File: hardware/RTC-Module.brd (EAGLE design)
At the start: 19.1 x 19.1 mm, 15 parts, among them Q1 32.768kHz, U1 DS1307

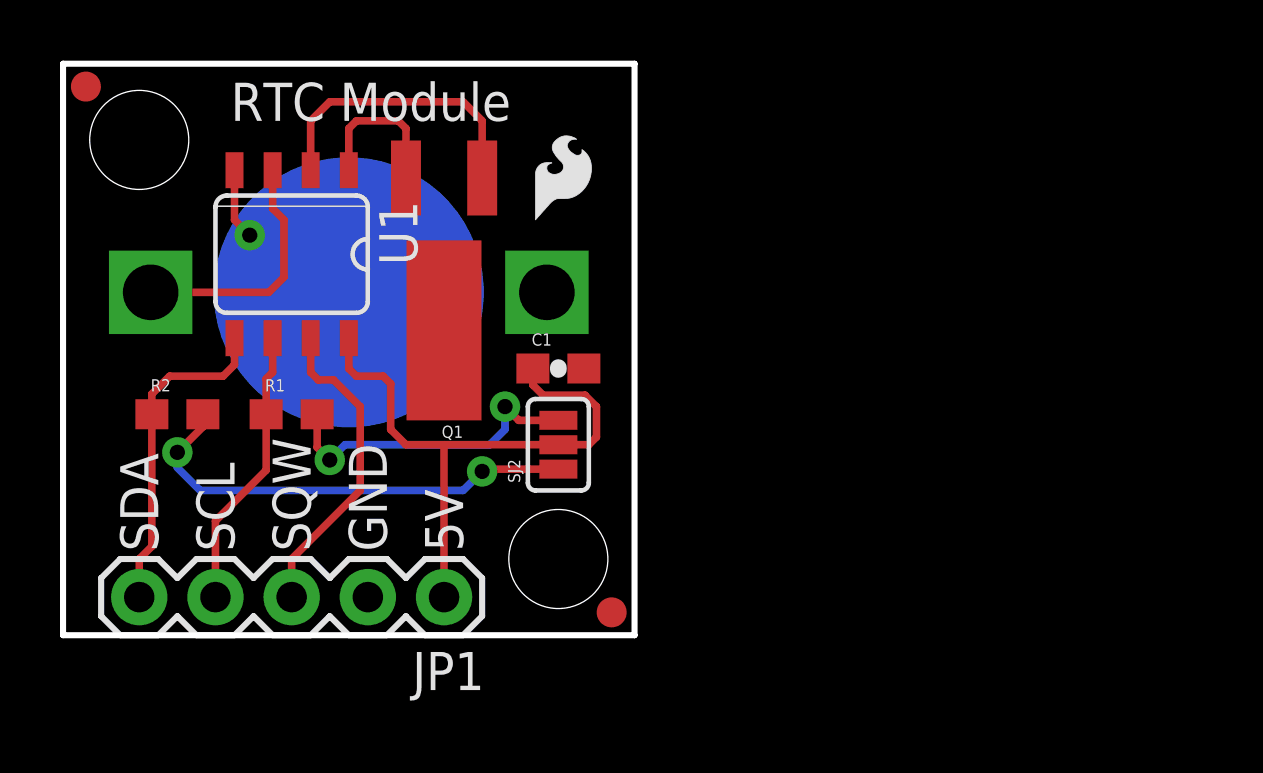
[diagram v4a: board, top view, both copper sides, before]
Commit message: Minor fixes
1.) added i2c address to sch
2.) added rev number in bottom copper
3.) updated revision info in sch and brd
4.) moved fiducials to clear drc
5.) cleaned up sda trace a bit
6.) added flame to bottom silk
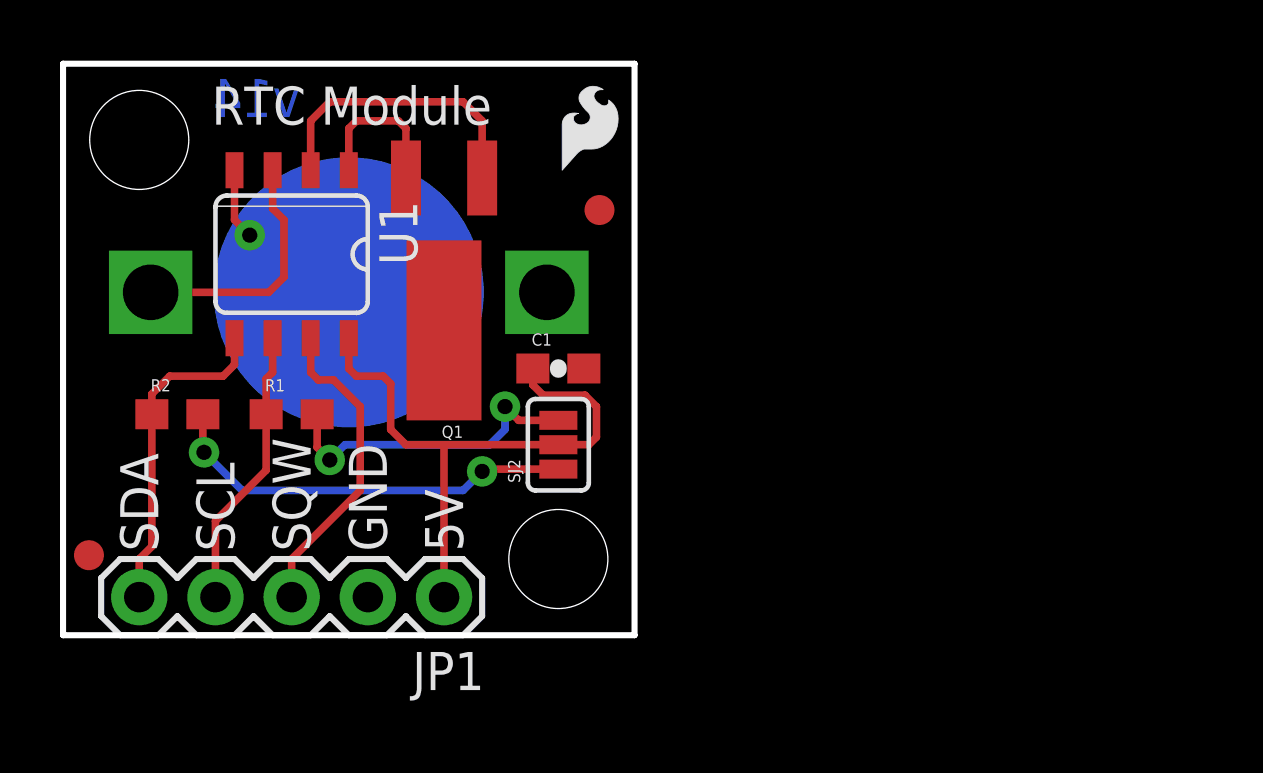
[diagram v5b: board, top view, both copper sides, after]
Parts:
- added U$2: LOGO-SFESK, SparkFun:SFE-LOGO-FLAME
- moved E$1 15.6 mm to (0.86, 2.67)
- moved E$2 13.4 mm to (17.9, 14.2)
- moved U$1 1.88 mm to (16.6, 15.5)
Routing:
- net N$6: track 15.4 -> 13.9 mm
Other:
- board text added: "Revised by: N. Seidle & Kade Jensen"
- board text added: "v14"
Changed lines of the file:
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@@
 <layer number="47" name="Measures" color="7" fill="1" visible="no" active="yes"/>
 <layer number="48" name="Document" color="7" fill="1" visible="no" active="yes"/>
-<layer number="49" name="Reference" color="7" fill="1" visible="no" active="yes"/>
+<layer number="49" name="Reference" color="7" fill="1" visible="yes" active="yes"/>
 <layer number="50" name="dxf" color="7" fill="1" visible="no" active="yes"/>
 <layer number="51" name="tDocu" color="6" fill="1" visible="yes" active="yes"/>
@@
 <text x="5.715" y="2.794" size="1.27" layer="21" font="vector" ratio="15" rot="R90">SCL</text>
 <text x="3.175" y="2.794" size="1.27" layer="21" font="vector" ratio="15" rot="R90">SDA</text>
-<text x="5.588" y="17.145" size="1.27" layer="21" font="vector" ratio="15">RTC Module</text>
+<text x="4.953" y="17.018" size="1.27" layer="21" font="vector" ratio="15">RTC Module</text>
 <text x="16.764" y="7.112" size="0.2032" layer="27">.1 uF</text>
-<text x="53.34" y="-15.24" size="1.778" layer="51" font="vector" ratio="15">N. Seidle</text>
+<text x="47.498" y="-15.24" size="1.778" layer="51" ratio="15">N. Seidle</text>
 <text x="12.954" y="3.175" size="1.27" layer="22" font="vector" ratio="15" rot="MR0">DS1307</text>
+<text x="34.29" y="-17.78" size="1.778" layer="51" ratio="15">Revised by: N. Seidle &amp; Kade Jensen</text>
+<text x="7.9121" y="17.272" size="1.27" layer="16" font="vector" ratio="15" rot="MR0">v14</text>
 </plain>
 <attributes>
@@
 </class>
 </classes>
-<designrules name="SparkFun *">
+<designrules name="SparkFun-2-layer">
 <description language="en">&lt;b&gt;EAGLE Design Rules&lt;/b&gt;
 &lt;p&gt;
@@
 <param name="mdViaViaSameLayer" value="8mil"/>
 <param name="mnLayersViaInSmd" value="2"/>
-<param name="mdCopperDimension" value="10mil"/>
+<param name="mdCopperDimension" value="8mil"/>
 <param name="mdDrill" value="8mil"/>
 <param name="mdSmdStop" value="0mil"/>
-<param name="msWidth" value="8mil"/>
-<param name="msDrill" value="20mil"/>
+<param name="msWidth" value="7mil"/>
+<param name="msDrill" value="15mil"/>
 <param name="msMicroVia" value="9.99mm"/>
 <param name="msBlindViaRatio" value="0.5"/>
@@
 </autorouter>
 <elements>
-<element name="U$1" library="SparkFun" package="SFE-LOGO-FLAME" value="LOGO-SFESK" x="15.748" y="13.843"/>
+<element name="U$1" library="SparkFun" package="SFE-LOGO-FLAME" value="LOGO-SFESK" x="16.637" y="15.494"/>
 <element name="U$6" library="SparkFun" package="STAND-OFF" value="STAND-OFF" x="16.51" y="2.54"/>
 <element name="U$7" library="SparkFun" package="STAND-OFF" value="STAND-OFF" x="2.54" y="16.51"/>
@@
 <element name="Q1" library="SparkFun-FreqCtrl" package="CRYSTAL-32KHZ-SMD" value="32.768kHz" x="12.7" y="15.24" rot="R180"/>
 <element name="JP1" library="SparkFun" package="1X05" value="" x="12.7" y="1.27" rot="R180"/>
-<element name="E$1" library="SparkFun" package="FIDUCIAL-1X2" value="" x="0.762" y="18.288"/>
-<element name="E$2" library="SparkFun" package="FIDUCIAL-1X2" value="" x="18.288" y="0.762"/>
+<element name="E$1" library="SparkFun" package="FIDUCIAL-1X2" value="" x="0.8636" y="2.667"/>
+<element name="E$2" library="SparkFun" package="FIDUCIAL-1X2" value="" x="17.8816" y="14.1732"/>
 <element name="R1" library="SparkFun-Resistors" package="0603" value="4.7k" x="7.62" y="7.366">
 <attribute name="PROD_ID" value="RES-07857" x="7.62" y="7.366" size="1.778" layer="27" font="vector" ratio="15" display="off"/>
@@
 <element name="LOGO1" library="SparkFun-Aesthetics" package="OSHW-LOGO-S" value="OSHW-LOGOS" x="2.54" y="4.191" rot="MR0"/>
 <element name="SJ2" library="SparkFun-Passives" package="SJ_3_PASTE1&amp;2&amp;3" value="" x="16.51" y="6.35" rot="R90"/>
+<element name="U$2" library="SparkFun" package="SFE-LOGO-FLAME" value="LOGO-SFESK" x="18.161" y="15.494" rot="MR0"/>
 </elements>
 <signals>
@@
 <contactref element="SJ2" pad="1"/>
 <wire x1="16.51" y1="5.5372" x2="14.0462" y2="5.5372" width="0.254" layer="1"/>
-<wire x1="13.335" y1="4.826" x2="4.572" y2="4.826" width="0.254" layer="16"/>
 <wire x1="14.0462" y1="5.5372" x2="13.97" y2="5.461" width="0.254" layer="1"/>
 <via x="13.97" y="5.461" extent="1-16" drill="0.508"/>
 <wire x1="13.97" y1="5.461" x2="13.335" y2="4.826" width="0.254" layer="16"/>
-<via x="3.81" y="6.096" extent="1-16" drill="0.508"/>
-<wire x1="3.81" y1="6.096" x2="3.81" y2="5.588" width="0.254" layer="16"/>
-<wire x1="3.81" y1="5.588" x2="4.572" y2="4.826" width="0.254" layer="16"/>
-<wire x1="4.66" y1="7.366" x2="4.66" y2="6.946" width="0.254" layer="1"/>
-<wire x1="4.66" y1="6.946" x2="3.81" y2="6.096" width="0.254" layer="1"/>
+<via x="4.699" y="6.096" extent="1-16" drill="0.508"/>
+<wire x1="4.66" y1="7.366" x2="4.66" y2="6.135" width="0.254" layer="1"/>
+<wire x1="4.66" y1="6.135" x2="4.699" y2="6.096" width="0.254" layer="1"/>
+<wire x1="13.335" y1="4.826" x2="5.969" y2="4.826" width="0.254" layer="16"/>
+<wire x1="5.969" y1="4.826" x2="4.699" y2="6.096" width="0.254" layer="16"/>
 </signal>
 </signals>
